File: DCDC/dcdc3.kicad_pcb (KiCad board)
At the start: 2 copper layers, 42.5 x 49.7 mm, 30 parts, among them J1 Vin, J2 GND, J3 V12out, J4 GND, J5 Syncout, M1-1 30V 60A, M2-1 30V 35A

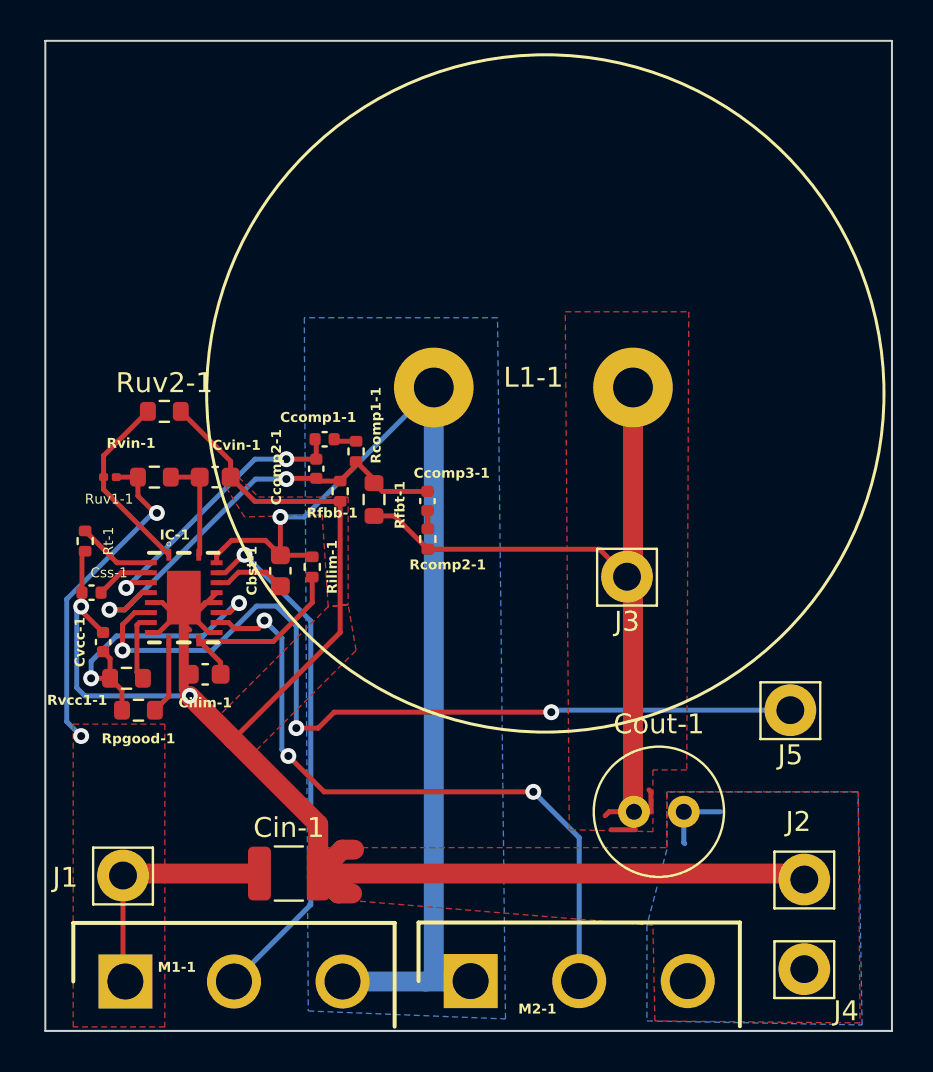
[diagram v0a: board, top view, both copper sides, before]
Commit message: restructured schematics, dumbed down pcb before redesign
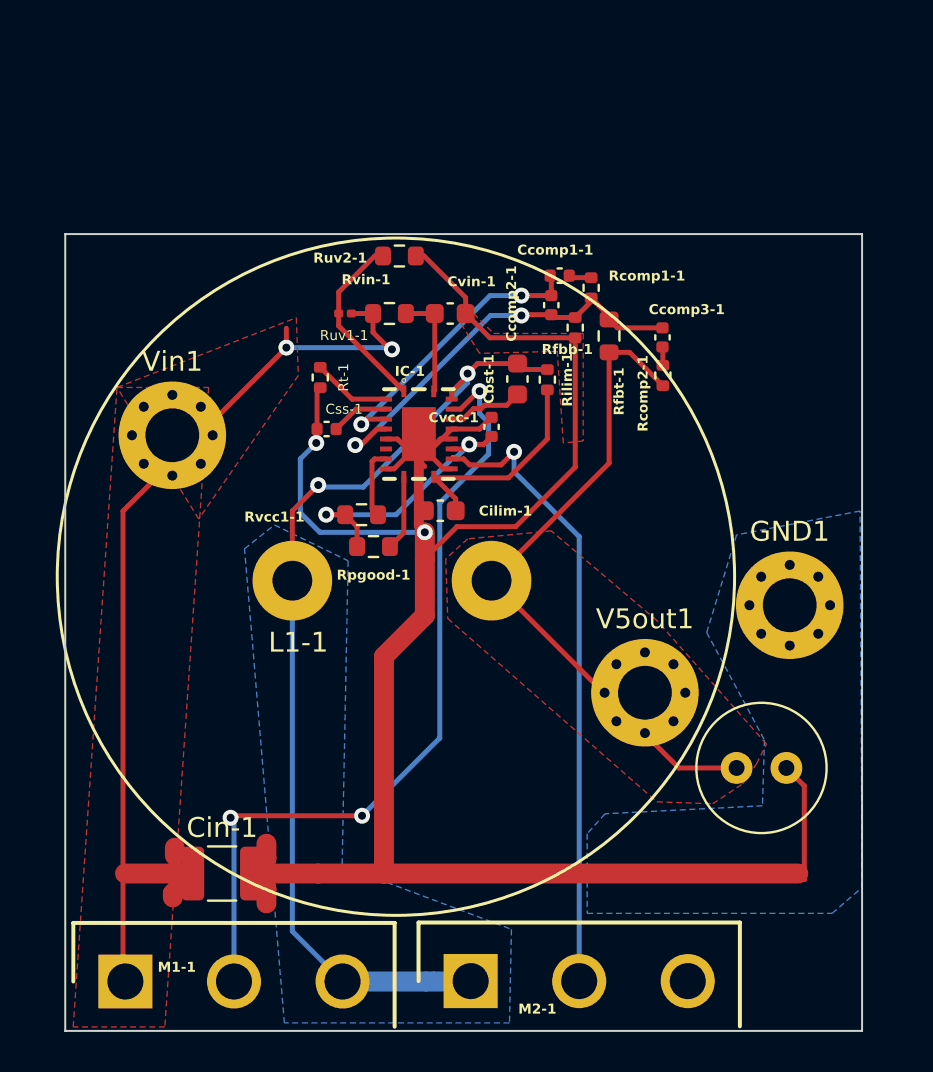
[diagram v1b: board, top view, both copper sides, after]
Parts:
- removed J1: Vin, Connector_Pin:Pin_D1.4mm_L8.5mm_W2.8mm_FlatFork
- removed J2, J4: GND, Connector_Pin:Pin_D1.4mm_L8.5mm_W2.8mm_FlatFork
- removed J3: V12out, Connector_Pin:Pin_D1.4mm_L8.5mm_W2.8mm_FlatFork
- removed J5: Syncout, Connector_Pin:Pin_D1.4mm_L8.5mm_W2.8mm_FlatFork
- added GND1: ~, MountingHole:MountingHole_2.7mm_M2.5_Pad_Via, F.Cu at (66.4, 98.6)
- added V5out1: ~, MountingHole:MountingHole_2.7mm_M2.5_Pad_Via, F.Cu at (59.1, 103.0)
- added Vin1: 12.5-22V, MountingHole:MountingHole_2.7mm_M2.5_Pad_Via, F.Cu at (35.4, 90.1)
- moved Cvcc-1 22.3 mm to (51.4, 89.7)
- moved Cbst-1 15.3 mm to (52.7, 87.3)
- moved Rilim-1 15.1 mm to (54.2, 87.3)
- moved Cvin-1 14.4 mm to (49.3, 84.0)
- moved Rpgood-1 14.4 mm to (45.5, 95.7)
- moved Ruv1-1 14.4 mm to (44.0, 84.0)
- moved Ccomp2-1 14.4 mm to (54.4, 83.6)
- moved Ccomp3-1 14.4 mm to (60.0, 85.2)
- moved Css-1 14.4 mm to (43.1, 89.8)
- moved IC-1 14.4 mm to (47.8, 90.0)
- moved Rcomp2-1 14.4 mm to (60.0, 87.1)
- moved Rfbt-1 14.4 mm to (57.3, 85.1)
- moved Rvin-1 14.4 mm to (46.3, 84.0)
- moved Cilim-1 14.4 mm to (48.8, 93.9)
- moved Rfbb-1 14.4 mm to (55.6, 84.7)
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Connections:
- net Net-(IC-1-AGND) renamed /12V/GND
- net Net-(J1-Pin_1) renamed /12V/Vin
- net Net-(J3-Pin_1) renamed /5V/V5out
- IC-1 pad 7: Net-(IC-1-SYNCOUT) -> unconnected-(IC-1-SYNCOUT-Pad7)
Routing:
- net Net-(IC-1-SYNCOUT): track 43.4 -> 0.00 mm, vias 3 -> 0
- net /12V/Vin: track 29.3 -> 50.9 mm
- net Net-(IC-1-HO): track 26.3 -> 41.0 mm, vias 1 -> 3
- net /12V/GND: track 98.2 -> 112.5 mm
- net /5V/V5out: track 40.9 -> 33.5 mm
- net Net-(IC-1-SW): track 54.7 -> 49.9 mm, vias 1 -> 2
- net Net-(IC-1-LO): track 33.9 -> 31.5 mm, vias 3 -> 1
- net Net-(IC-1-FB): track 22.7 -> 21.0 mm
- net Net-(IC-1-VCC): track 15.1 -> 13.7 mm
- net Net-(IC-1-ILIM): track 9.96 -> 11.3 mm
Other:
- board size 42.5 x 49.7 mm -> 40 x 40 mm

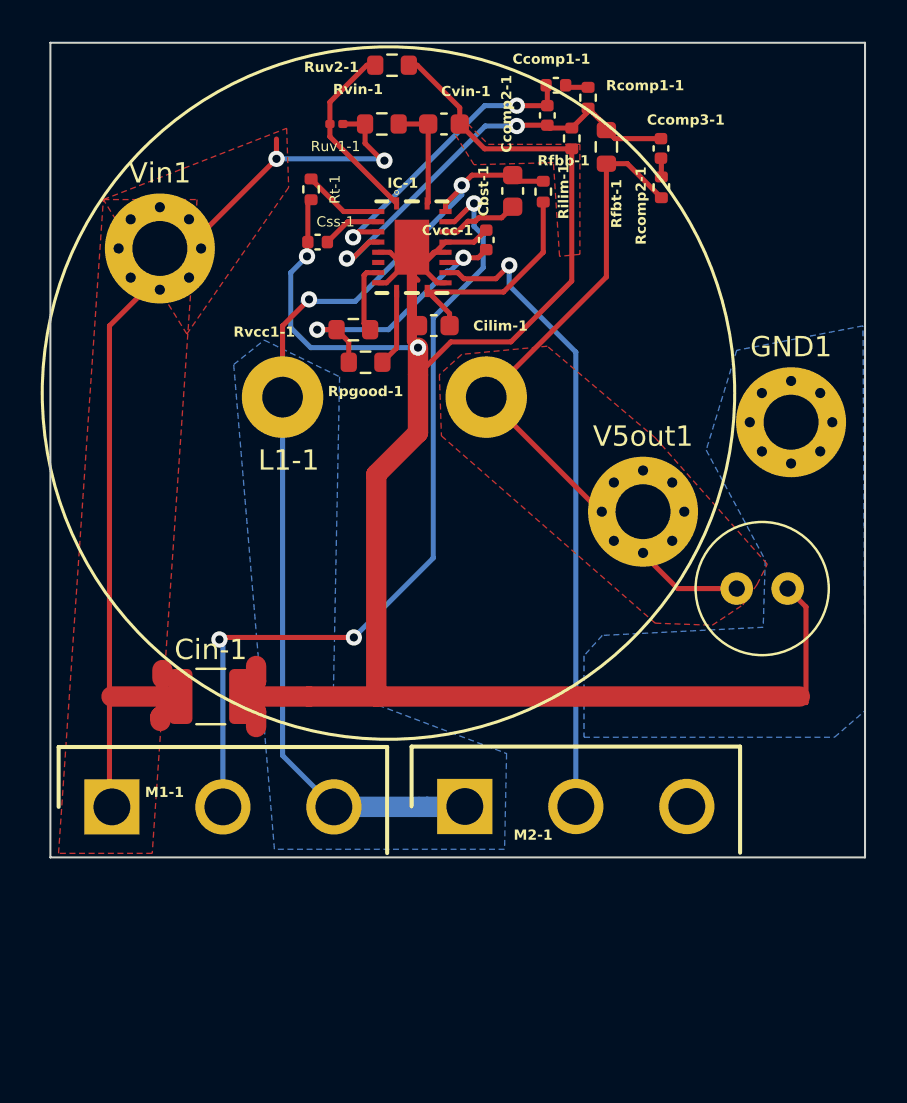
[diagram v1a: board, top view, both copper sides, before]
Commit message: pcb part for 5V ready
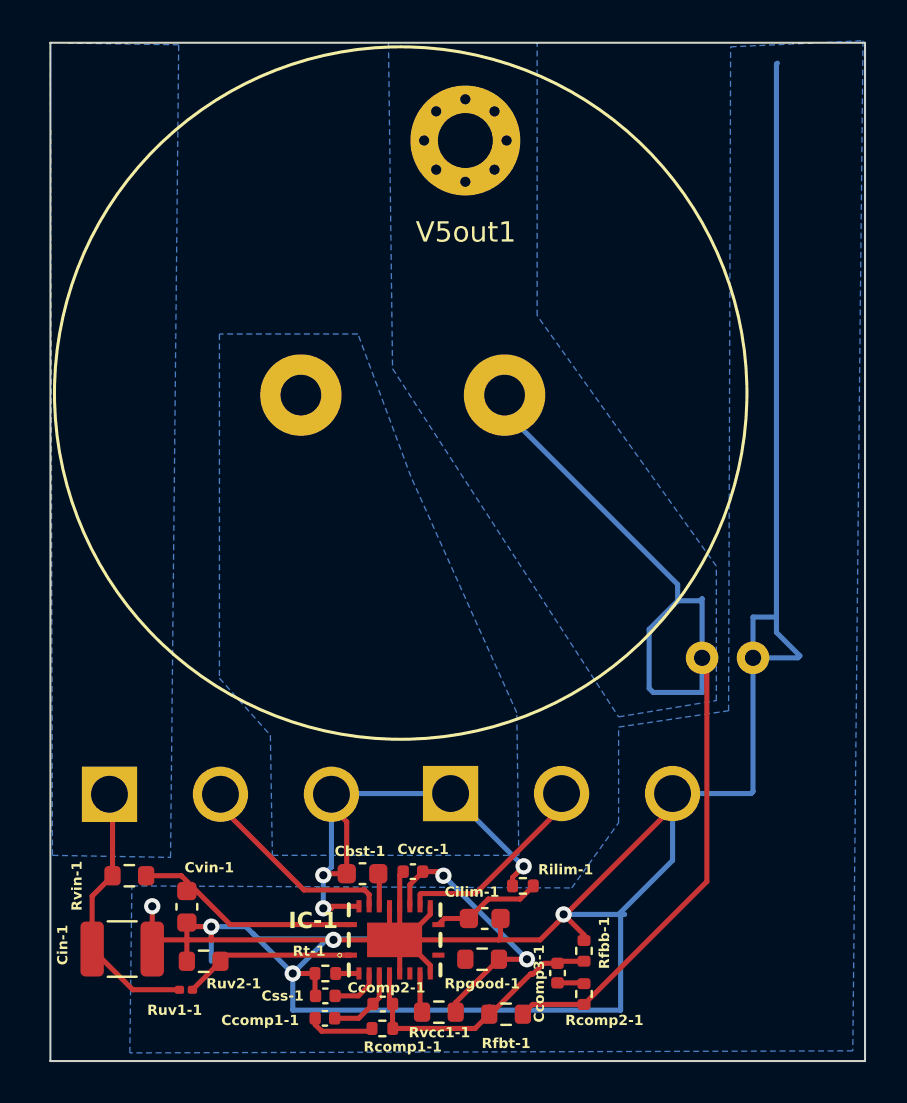
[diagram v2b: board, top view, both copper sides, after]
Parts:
- removed GND1: ~, MountingHole:MountingHole_2.7mm_M2.5_Pad_Via
- removed Vin1: 12.5-22V, MountingHole:MountingHole_2.7mm_M2.5_Pad_Via
- Cout-1, L1-1, M1-1, M2-1: moved to B.Cu
- moved Ccomp1-1 47.2 mm to (43.5, 127.9), turned to 0 degrees
- moved Rcomp1-1 46.8 mm to (46.3, 128.4), turned to 180 degrees
- moved Ruv2-1 45.0 mm to (37.5, 125.1), turned to 180 degrees
- moved Ccomp2-1 44.4 mm to (46.3, 127.2), turned to 180 degrees
- moved Ruv1-1 43.2 mm to (36.7, 126.5), turned to 0 degrees
- moved Rfbt-1 42.9 mm to (52.4, 127.7), turned to 180 degrees
- moved Ccomp3-1 40.8 mm to (54.9, 125.7)
- moved Cvin-1 40.5 mm to (36.7, 122.4), turned to -90 degrees
- moved Rfbb-1 39.9 mm to (56.2, 124.6), turned to 90 degrees
- moved Rcomp2-1 39.8 mm to (56.2, 126.7)
- moved Rvin-1 38.9 mm to (33.9, 120.9)
- moved Rt-1 38.5 mm to (43.5, 125.7), turned to 180 degrees
- moved Css-1 37.0 mm to (43.5, 126.8)
- moved Cbst-1 34.3 mm to (45.3, 120.8), turned to 180 degrees
- moved Rilim-1 34.1 mm to (53.2, 121.4), turned to 180 degrees
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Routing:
- net /12V/Vin: track 50.9 -> 13.2 mm, vias 2 -> 0
- net /12V/GND: track 112.5 -> 145.2 mm, vias 2 -> 5
- net Net-(IC-1-HO): track 41.0 -> 9.67 mm, vias 3 -> 0
- net Net-(IC-1-SW): track 49.9 -> 24.3 mm, vias 2 -> 3
- net Net-(IC-1-LO): track 31.5 -> 9.37 mm, vias 1 -> 0
- net /5V/V5out: track 33.5 -> 50.2 mm
- net Net-(IC-1-COMP): track 14.7 -> 3.80 mm, vias 2 -> 0
- net Net-(IC-1-FB): track 21.0 -> 13.9 mm, vias 2 -> 0
- net Net-(IC-1-ILIM): track 11.3 -> 5.45 mm
- net Net-(IC-1-VIN): track 5.37 -> 11.0 mm
- net Net-(IC-1-PGOOD): track 3.79 -> 0.00 mm
- net Net-(IC-1-RT): track 3.96 -> 1.14 mm
- net Net-(IC-1-BST): track 3.81 -> 1.62 mm
- net Net-(Ccomp1-1-Pad1): track 1.14 -> 3.29 mm
- net Net-(IC-1-SYNCIN): track 3.55 -> 1.94 mm
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- added copper zone on B.Cu, net /12V/Vin
- added copper zone on B.Cu, net /5V/V5out
- removed copper zone on F.Cu, net /12V/GND
- removed copper zone on F.Cu, net /12V/Vin
- removed copper zone on F.Cu, net /5V/V5out
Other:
- board size 40 x 40 mm -> 40 x 50 mm

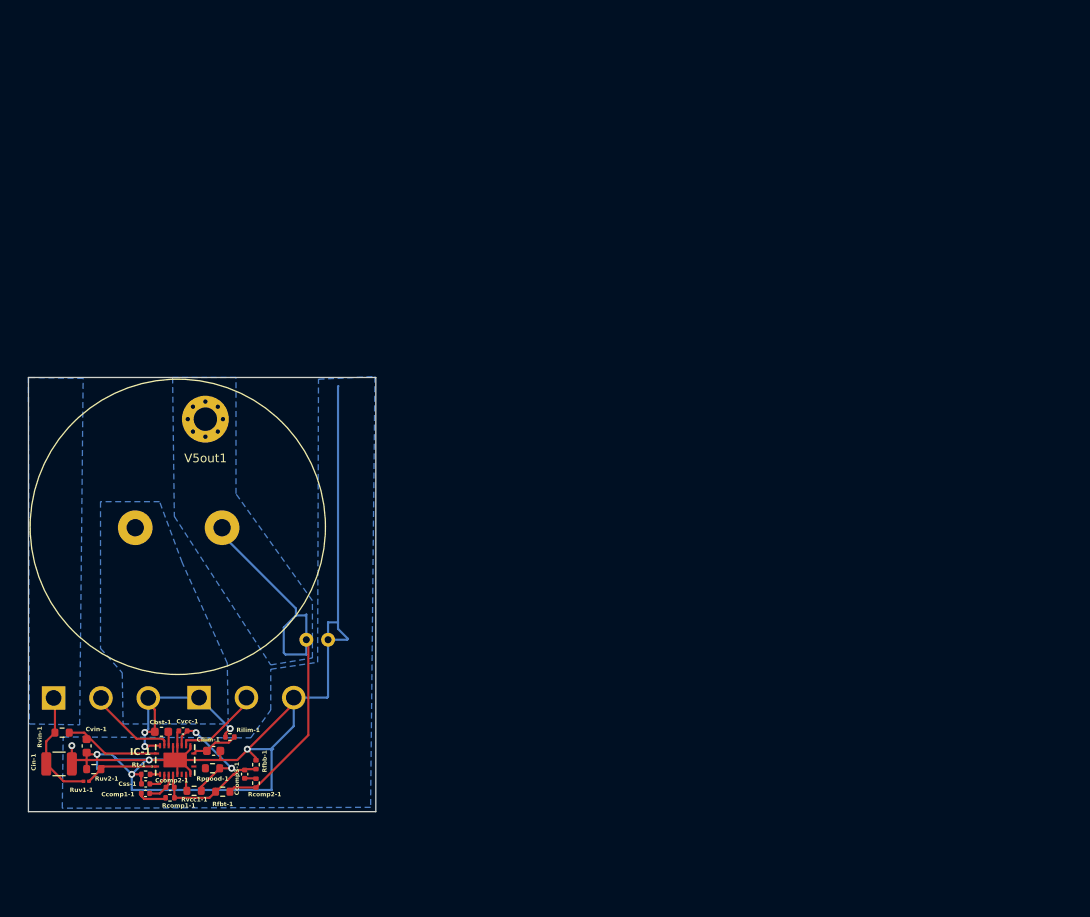
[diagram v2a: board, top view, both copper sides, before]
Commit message: pcb updated with all parts
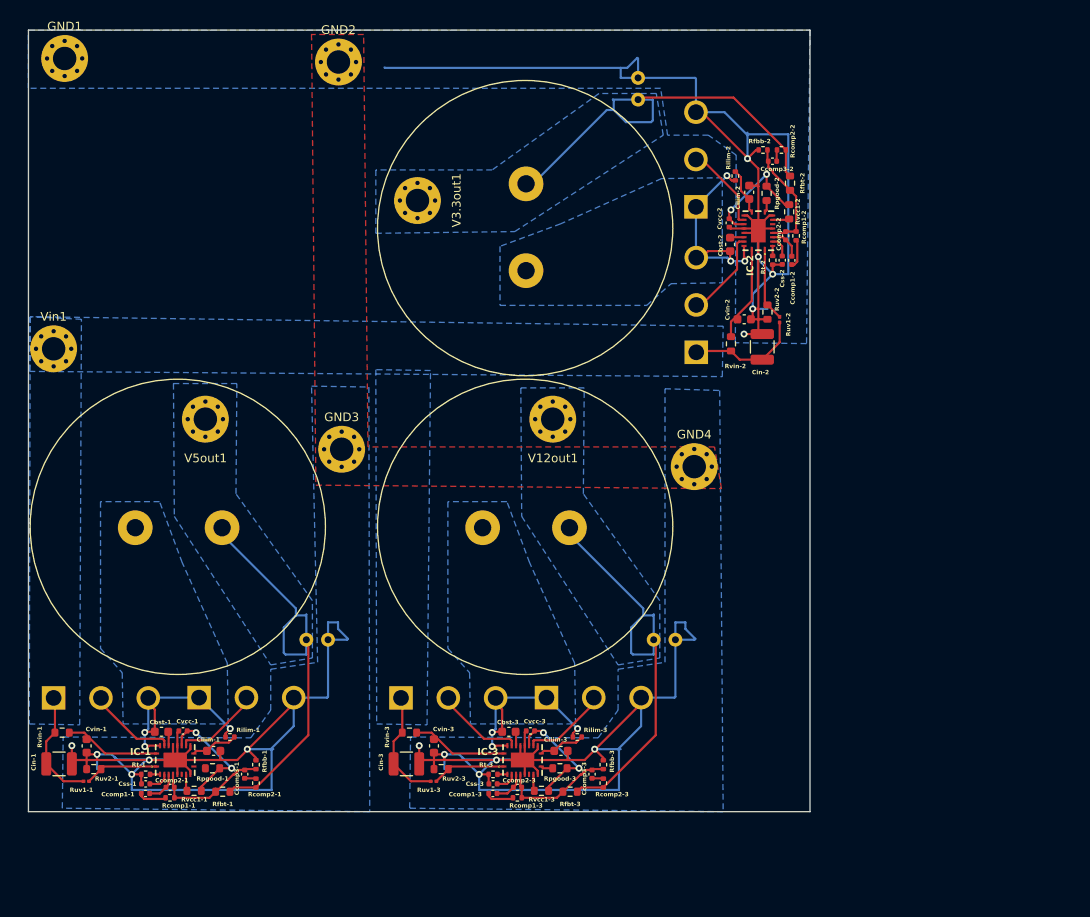
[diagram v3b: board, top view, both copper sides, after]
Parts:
- added Cbst-2: 100 n, Capacitor_SMD:C_0603_1608Metric, F.Cu at (110.8, 64.7)
- added Cbst-3: 100 n, Capacitor_SMD:C_0603_1608Metric, F.Cu at (85.3, 120.8)
- added Ccomp1-2: 15 nF, Capacitor_SMD:C_0402_1005Metric, F.Cu at (117.9, 66.5)
- added Ccomp1-3: 15 nF, Capacitor_SMD:C_0402_1005Metric, F.Cu at (83.5, 127.9)
- added Ccomp2-2: 1.2 n, Capacitor_SMD:C_0402_1005Metric, F.Cu at (117.2, 63.7)
- added Ccomp2-3: 1.2 n, Capacitor_SMD:C_0402_1005Metric, F.Cu at (86.3, 127.2)
- added Ccomp3-2: 910 p, Capacitor_SMD:C_0402_1005Metric, F.Cu at (115.7, 55.1)
- added Ccomp3-3: 910 p, Capacitor_SMD:C_0402_1005Metric, F.Cu at (94.9, 125.7)
- added Cilim-2: 10 p, Capacitor_SMD:C_0603_1608Metric, F.Cu at (113.0, 58.7)
- added Cilim-3: 10 p, Capacitor_SMD:C_0603_1608Metric, F.Cu at (91.3, 123.0)
- added Cin-2: 4.7 uF, Capacitor_SMD:C_1210_3225Metric, F.Cu at (114.5, 76.5)
- added Cin-3: 4.7 uF, Capacitor_SMD:C_1210_3225Metric, F.Cu at (73.5, 124.5)
- added Cout-2: 56 u, Capacitor_THT:C_Radial_D6.3mm_H5.0mm_P2.50mm, B.Cu at (100.2, 48.0)
- added Cout-3: 56 u, Capacitor_THT:C_Radial_D6.3mm_H5.0mm_P2.50mm, B.Cu at (102.0, 110.2)
- added Css-2: 56n, Capacitor_SMD:C_0402_1005Metric, F.Cu at (116.8, 66.5)
- added Css-3: 56n, Capacitor_SMD:C_0402_1005Metric, F.Cu at (83.5, 126.8)
- added Cvcc-2: 2.2 u, Capacitor_SMD:C_0402_1005Metric, F.Cu at (110.7, 62.2)
- added Cvcc-3: 2.2 u, Capacitor_SMD:C_0402_1005Metric, F.Cu at (87.8, 120.7)
- added Cvin-2: 100 nF, Capacitor_SMD:C_0603_1608Metric, F.Cu at (112.4, 73.3)
- added Cvin-3: 100 nF, Capacitor_SMD:C_0603_1608Metric, F.Cu at (76.7, 122.4)
- added GND1: ~, MountingHole:MountingHole_2.7mm_M2.5_Pad_Via, F.Cu at (34.2, 43.3)
- added GND2: ~, MountingHole:MountingHole_2.7mm_M2.5_Pad_Via, F.Cu at (65.7, 43.7)
- added GND3: ~, MountingHole:MountingHole_2.7mm_M2.5_Pad_Via, F.Cu at (66.1, 88.3)
- added GND4: ~, MountingHole:MountingHole_2.7mm_M2.5_Pad_Via, F.Cu at (106.7, 90.3)
- added IC-2: LM5145RGYR, Library:RGY0020B, F.Cu at (114.0, 63.1)
- added IC-3: LM5145RGYR, Library:RGY0020B, F.Cu at (86.9, 124.0)
- added L1-2: 4.7 u, Library:A3mmCoil, B.Cu at (87.3, 62.7)
- added L1-3: 4.7 u, Library:A3mmCoil, B.Cu at (87.3, 97.3)
- added M1-2: 30V 60A, Library:TO545P521X1594X2566-3P, B.Cu at (106.9, 77.1)
- added M1-3: 30V 60A, Library:TO545P521X1594X2566-3P, B.Cu at (72.9, 116.9)
- added M2-2: 30V 35A, Library:TO545P521X1594X2566-3P, B.Cu at (106.9, 60.4)
- added M2-3: 30V 35A, Library:TO545P521X1594X2566-3P, B.Cu at (89.7, 116.9)
- added Rcomp1-2: 1.78 k, Resistor_SMD:R_0402_1005Metric, F.Cu at (118.4, 63.7)
- added Rcomp1-3: 1.78 k, Resistor_SMD:R_0402_1005Metric, F.Cu at (86.3, 128.4)
- added Rcomp2-2: 1.82 k, Resistor_SMD:R_0402_1005Metric, F.Cu at (116.7, 53.8)
- added Rcomp2-3: 1.82 k, Resistor_SMD:R_0402_1005Metric, F.Cu at (96.2, 126.7)
- added Rfbb-2: 1.27 k, Resistor_SMD:R_0402_1005Metric, F.Cu at (114.6, 53.8)
- added Rfbb-3: 1.27 k, Resistor_SMD:R_0402_1005Metric, F.Cu at (96.2, 124.6)
- added Rfbt-2: 18 k, Resistor_SMD:R_0603_1608Metric, F.Cu at (117.7, 57.6)
- added Rfbt-3: 18 k, Resistor_SMD:R_0603_1608Metric, F.Cu at (92.4, 127.7)
- added Rilim-2: 619, Resistor_SMD:R_0402_1005Metric, F.Cu at (111.4, 56.8)
- added Rilim-3: 619, Resistor_SMD:R_0402_1005Metric, F.Cu at (93.2, 121.4)
- added Rpgood-2: 20 k, Resistor_SMD:R_0603_1608Metric, F.Cu at (115.0, 58.8)
- added Rpgood-3: 20 k, Resistor_SMD:R_0603_1608Metric, F.Cu at (91.2, 125.0)
- added Rt-2: 69.8k, Resistor_SMD:R_0402_1005Metric, F.Cu at (115.7, 66.5)
- added Rt-3: 69.8k, Resistor_SMD:R_0402_1005Metric, F.Cu at (83.5, 125.7)
- added Ruv1-2: 68.1k, Resistor_SMD:R_0201_0603Metric, F.Cu at (116.5, 73.3)
- added Ruv1-3: 68.1k, Resistor_SMD:R_0201_0603Metric, F.Cu at (76.7, 126.5)
- added Ruv2-2: 9.1 k, Resistor_SMD:R_0603_1608Metric, F.Cu at (115.1, 72.5)
- added Ruv2-3: 9.1 k, Resistor_SMD:R_0603_1608Metric, F.Cu at (77.5, 125.1)
- added Rvcc1-2: 20 k, Resistor_SMD:R_0603_1608Metric, F.Cu at (117.6, 60.9)
- added Rvcc1-3: 20 k, Resistor_SMD:R_0603_1608Metric, F.Cu at (89.1, 127.6)
- added Rvin-2: 2.1, Resistor_SMD:R_0603_1608Metric, F.Cu at (110.9, 76.1)
- added Rvin-3: 2.1, Resistor_SMD:R_0603_1608Metric, F.Cu at (73.9, 120.9)
- added V12out1: ~, MountingHole:MountingHole_2.7mm_M2.5_Pad_Via, F.Cu at (90.4, 84.8)
- added V3.3out1: ~, MountingHole:MountingHole_2.7mm_M2.5_Pad_Via, F.Cu at (74.8, 59.6)
- added Vin1: 12.5-22V, MountingHole:MountingHole_2.7mm_M2.5_Pad_Via, F.Cu at (32.9, 76.7)
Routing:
- net /12V/GND: track 145.2 -> 381.1 mm, vias 5 -> 15
- net /3.3V/V3.3out: track 0.00 -> 50.2 mm
- net /12V/V12out: track 0.00 -> 50.2 mm
- net Net-(IC-2-SW): track 0.00 -> 24.3 mm, vias 0 -> 3
- net Net-(IC-3-SW): track 0.00 -> 24.3 mm, vias 0 -> 3
- net Net-(IC-2-FB): track 0.00 -> 13.9 mm
- net Net-(IC-3-FB): track 0.00 -> 13.9 mm
- net Net-(IC-2-VCC): track 0.00 -> 13.5 mm, vias 0 -> 2
- net Net-(IC-3-VCC): track 0.00 -> 13.5 mm, vias 0 -> 2
- net /12V/Vin: track 13.2 -> 26.4 mm
- net Net-(M1-3-D): track 0.00 -> 13.2 mm
- net Net-(IC-3-VIN): track 0.00 -> 11.0 mm
- net Net-(IC-2-VIN): track 0.00 -> 11.0 mm
- net Net-(IC-3-HO): track 0.00 -> 9.67 mm
- net Net-(IC-2-HO): track 0.00 -> 9.67 mm
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- added copper zone on F.Cu, net /12V/GND
- added copper zone on B.Cu, net /12V/V12out
- added copper zone on B.Cu, net /3.3V/V3.3out
- added copper zone on B.Cu, net Net-(IC-2-SW)
- added copper zone on B.Cu, net Net-(IC-3-SW)
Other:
- board size 40 x 50 mm -> 90 x 90 mm
